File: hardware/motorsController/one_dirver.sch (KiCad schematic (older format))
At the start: 9 parts

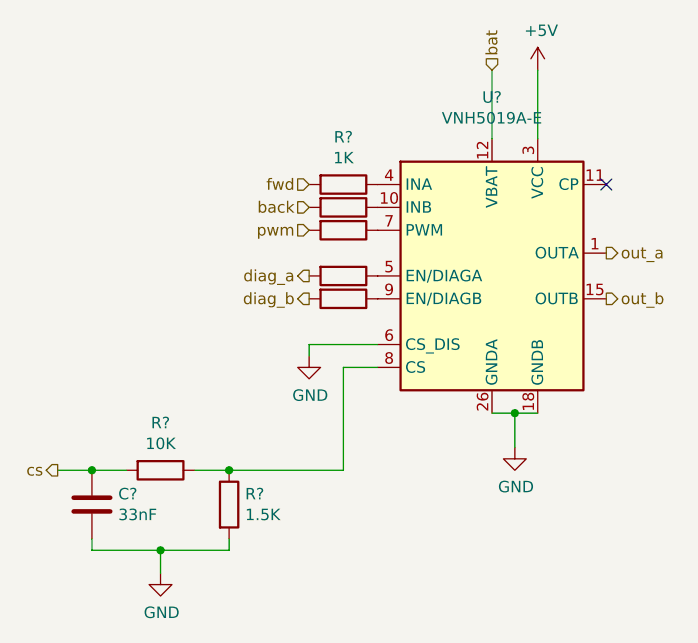
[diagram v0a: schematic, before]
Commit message: layout a pcb for the motor driver IC
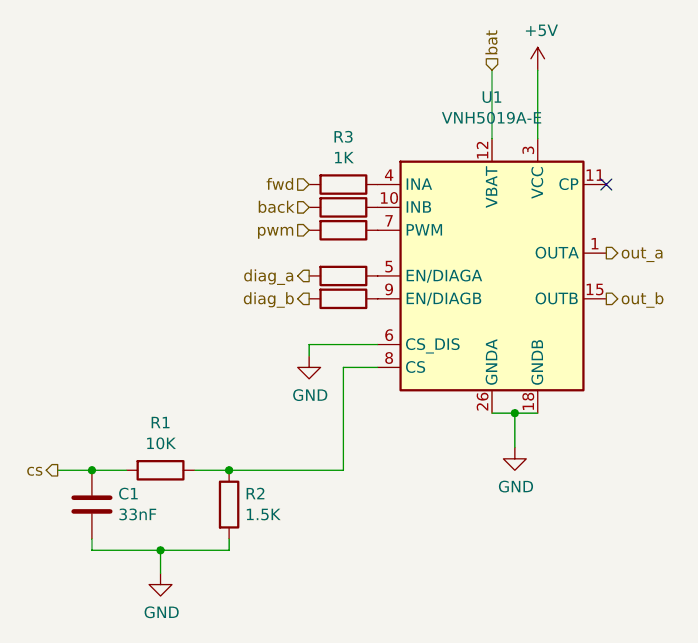
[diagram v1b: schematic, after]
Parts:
- C1: renamed from C?; footprint (none) -> Capacitor_SMD:C_1206_3216Metric
- R1, R2, R3, R4, R5, R6, R7: renamed from R?; footprint (none) -> Resistor_SMD:R_0805_2012Metric
- gave numbers to parts that had none: 1
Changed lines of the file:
@@
 $EndDescr
 $Comp
-L Driver_Motor:VNH5019A-E U?
+L Driver_Motor:VNH5019A-E U1
 U 1 1 5F75DD74
 P 3150 2750
-F 0 "U?" H 3150 3531 50  0000 C CNN
+F 0 "U1" H 3150 3531 50  0000 C CNN
 F 1 "VNH5019A-E" H 3150 3440 50  0000 C CNN
 F 2 "Package_SO:ST_MultiPowerSO-30" H 4050 2200 50  0001 C CNN
@@
 	3250 3350 3350 3350
 $Comp
-L Device:R R?
+L Device:R R3
 U 1 1 5F764A13
 P 2500 2350
-F 0 "R?" V 2293 2350 50  0000 C CNN
+F 0 "R3" V 2293 2350 50  0000 C CNN
 F 1 "1K" V 2384 2350 50  0000 C CNN
-F 2 "" V 2430 2350 50  0001 C CNN
+F 2 "Resistor_SMD:R_0805_2012Metric" V 2430 2350 50  0001 C CNN
 F 3 "~" H 2500 2350 50  0001 C CNN
 	1    2500 2350
@@
 $EndComp
 $Comp
-L Device:R R?
+L Device:R R4
 U 1 1 5F765406
 P 2500 2450
-F 0 "R?" V 2293 2450 50  0001 C CNN
+F 0 "R4" V 2293 2450 50  0001 C CNN
 F 1 "1K" V 2384 2450 50  0001 C CNN
-F 2 "" V 2430 2450 50  0001 C CNN
+F 2 "Resistor_SMD:R_0805_2012Metric" V 2430 2450 50  0001 C CNN
 F 3 "~" H 2500 2450 50  0001 C CNN
 	1    2500 2450
@@
 $EndComp
 $Comp
-L Device:R R?
+L Device:R R5
 U 1 1 5F7658F2
 P 2500 2550
-F 0 "R?" V 2293 2550 50  0001 C CNN
+F 0 "R5" V 2293 2550 50  0001 C CNN
 F 1 "1K" V 2384 2550 50  0001 C CNN
-F 2 "" V 2430 2550 50  0001 C CNN
+F 2 "Resistor_SMD:R_0805_2012Metric" V 2430 2550 50  0001 C CNN
 F 3 "~" H 2500 2550 50  0001 C CNN
 	1    2500 2550
@@
 pwm
 $Comp
-L Device:R R?
+L Device:R R6
 U 1 1 5F77E0ED
 P 2500 2750
-F 0 "R?" V 2293 2750 50  0001 C CNN
+F 0 "R6" V 2293 2750 50  0001 C CNN
 F 1 "1K" V 2384 2750 50  0001 C CNN
-F 2 "" V 2430 2750 50  0001 C CNN
+F 2 "Resistor_SMD:R_0805_2012Metric" V 2430 2750 50  0001 C CNN
 F 3 "~" H 2500 2750 50  0001 C CNN
 	1    2500 2750
@@
 diag_a
 $Comp
-L Device:R R?
+L Device:R R7
 U 1 1 5F781639
 P 2500 2850
-F 0 "R?" V 2293 2850 50  0001 C CNN
+F 0 "R7" V 2293 2850 50  0001 C CNN
 F 1 "1K" V 2384 2850 50  0001 C CNN
-F 2 "" V 2430 2850 50  0001 C CNN
+F 2 "Resistor_SMD:R_0805_2012Metric" V 2430 2850 50  0001 C CNN
 F 3 "~" H 2500 2850 50  0001 C CNN
 	1    2500 2850
@@
 diag_b
 $Comp
-L power:GND #PWR?
+L power:GND #PWR0101
 U 1 1 5F781B76
 P 2350 3100
-F 0 "#PWR?" H 2350 2850 50  0001 C CNN
+F 0 "#PWR0101" H 2350 2850 50  0001 C CNN
 F 1 "GND" H 2355 2927 50  0000 C CNN
 F 2 "" H 2350 3100 50  0001 C CNN
@@
 	2350 3050 2650 3050
 $Comp
-L Device:R R?
+L Device:R R2
 U 1 1 5F782890
 P 2000 3750
-F 0 "R?" H 2070 3796 50  0000 L CNN
+F 0 "R2" H 2070 3796 50  0000 L CNN
 F 1 "1.5K" H 2070 3705 50  0000 L CNN
-F 2 "" V 1930 3750 50  0001 C CNN
+F 2 "Resistor_SMD:R_0805_2012Metric" V 1930 3750 50  0001 C CNN
 F 3 "~" H 2000 3750 50  0001 C CNN
 	1    2000 3750
@@
 $EndComp
 $Comp
-L power:GND #PWR?
+L power:GND #PWR0102
 U 1 1 5F783B44
 P 1700 4050
-F 0 "#PWR?" H 1700 3800 50  0001 C CNN
+F 0 "#PWR0102" H 1700 3800 50  0001 C CNN
 F 1 "GND" H 1705 3877 50  0000 C CNN
 F 2 "" H 1700 4050 50  0001 C CNN
@@
 $EndComp
 $Comp
-L Device:R R?
+L Device:R R1
 U 1 1 5F7841BA
 P 1700 3600
-F 0 "R?" V 1493 3600 50  0000 C CNN
+F 0 "R1" V 1493 3600 50  0000 C CNN
 F 1 "10K" V 1584 3600 50  0000 C CNN
-F 2 "" V 1630 3600 50  0001 C CNN
+F 2 "Resistor_SMD:R_0805_2012Metric" V 1630 3600 50  0001 C CNN
 F 3 "~" H 1700 3600 50  0001 C CNN
 	1    1700 3600
@@
 Connection ~ 2000 3600
 $Comp
-L Device:C C?
+L Device:C C1
 U 1 1 5F784D90
 P 1400 3750
-F 0 "C?" H 1515 3796 50  0000 L CNN
+F 0 "C1" H 1515 3796 50  0000 L CNN
 F 1 "33nF" H 1515 3705 50  0000 L CNN
-F 2 "" H 1438 3600 50  0001 C CNN
+F 2 "Capacitor_SMD:C_1206_3216Metric" H 1438 3600 50  0001 C CNN
 F 3 "~" H 1400 3750 50  0001 C CNN
 	1    1400 3750
@@
 bat
 $Comp
-L power:+5V #PWR?
+L power:+5V #PWR0103
 U 1 1 5F78A1BC
 P 3350 1850
-F 0 "#PWR?" H 3350 1700 50  0001 C CNN
+F 0 "#PWR0103" H 3350 1700 50  0001 C CNN
 F 1 "+5V" H 3365 2023 50  0000 C CNN
 F 2 "" H 3350 1850 50  0001 C CNN
@@
 	2000 3600 2500 3600
 $Comp
-L power:GND #PWR?
+L power:GND #PWR0104
 U 1 1 5F794080
 P 3250 3500
-F 0 "#PWR?" H 3250 3250 50  0001 C CNN
+F 0 "#PWR0104" H 3250 3250 50  0001 C CNN
 F 1 "GND" H 3255 3327 50  0000 C CNN
 F 2 "" H 3250 3500 50  0001 C CNN
